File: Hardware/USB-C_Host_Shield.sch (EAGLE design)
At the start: 23 parts, among them U1 ARDUINO_UNO_R3_SHIELDBASIC, U4 AP7361C-33FGEUDFN-8, U5 MAX3421

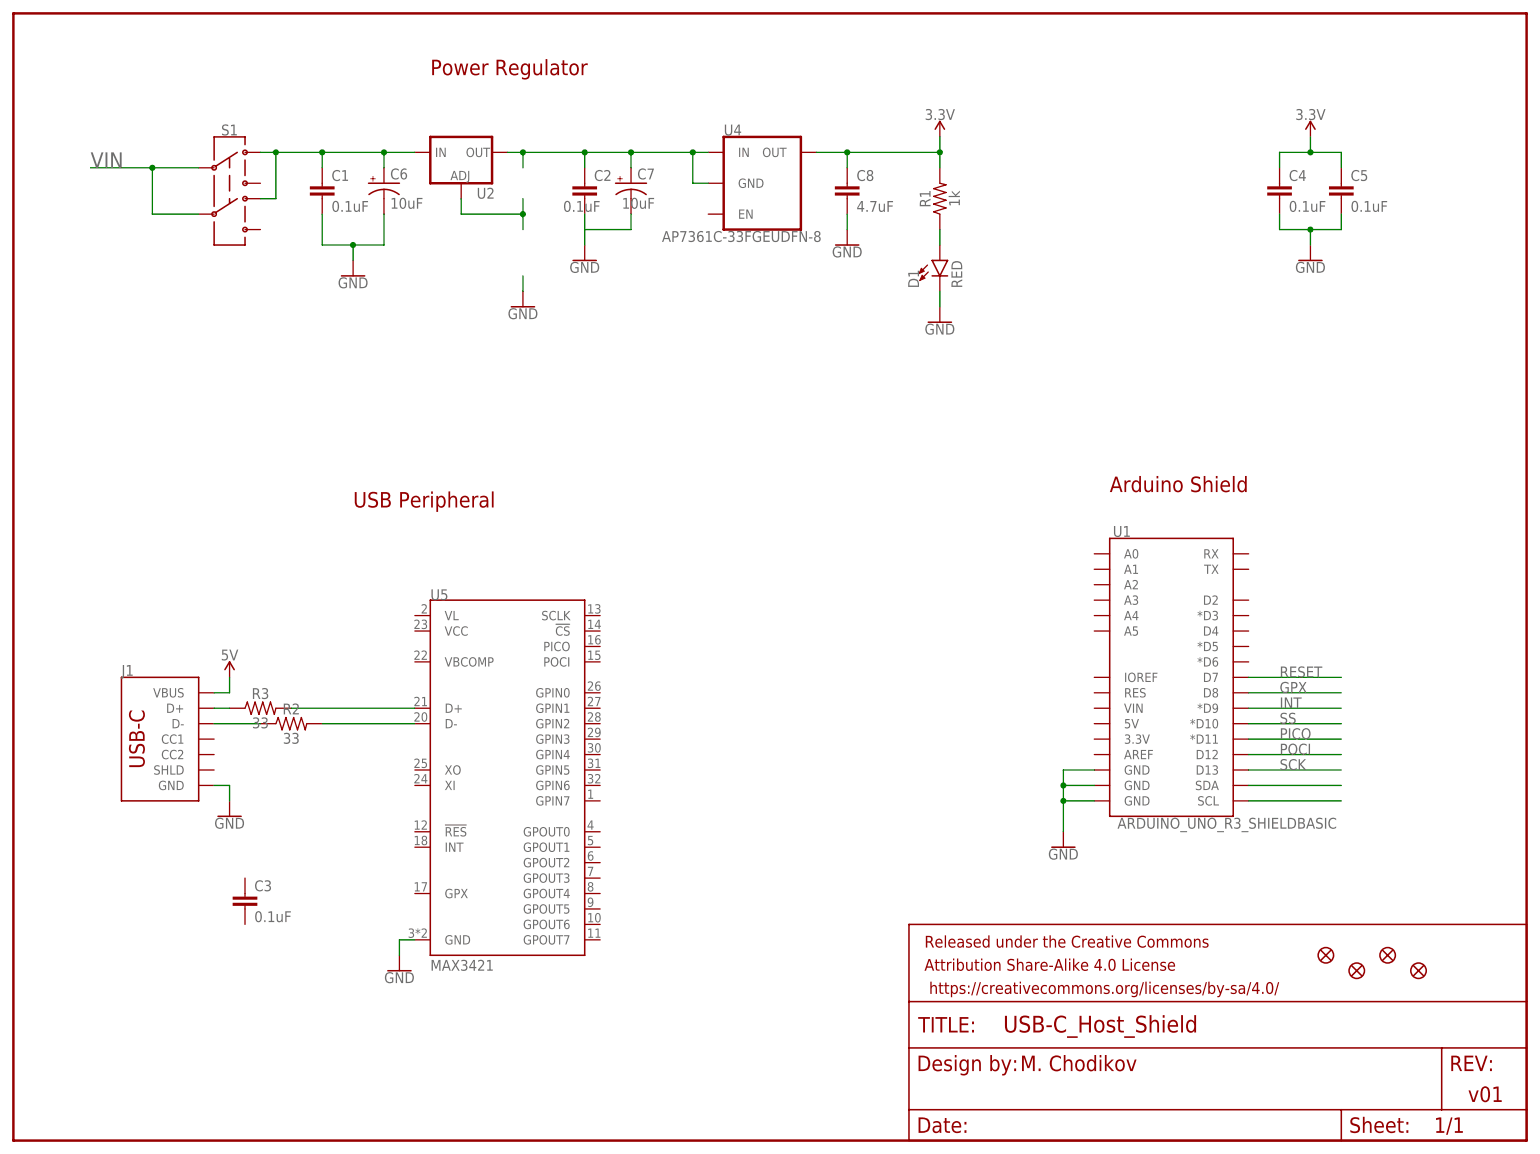
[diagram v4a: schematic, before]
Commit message: Updates to schematic, added documents
Continued work on schematic, added programming guide to documents folder
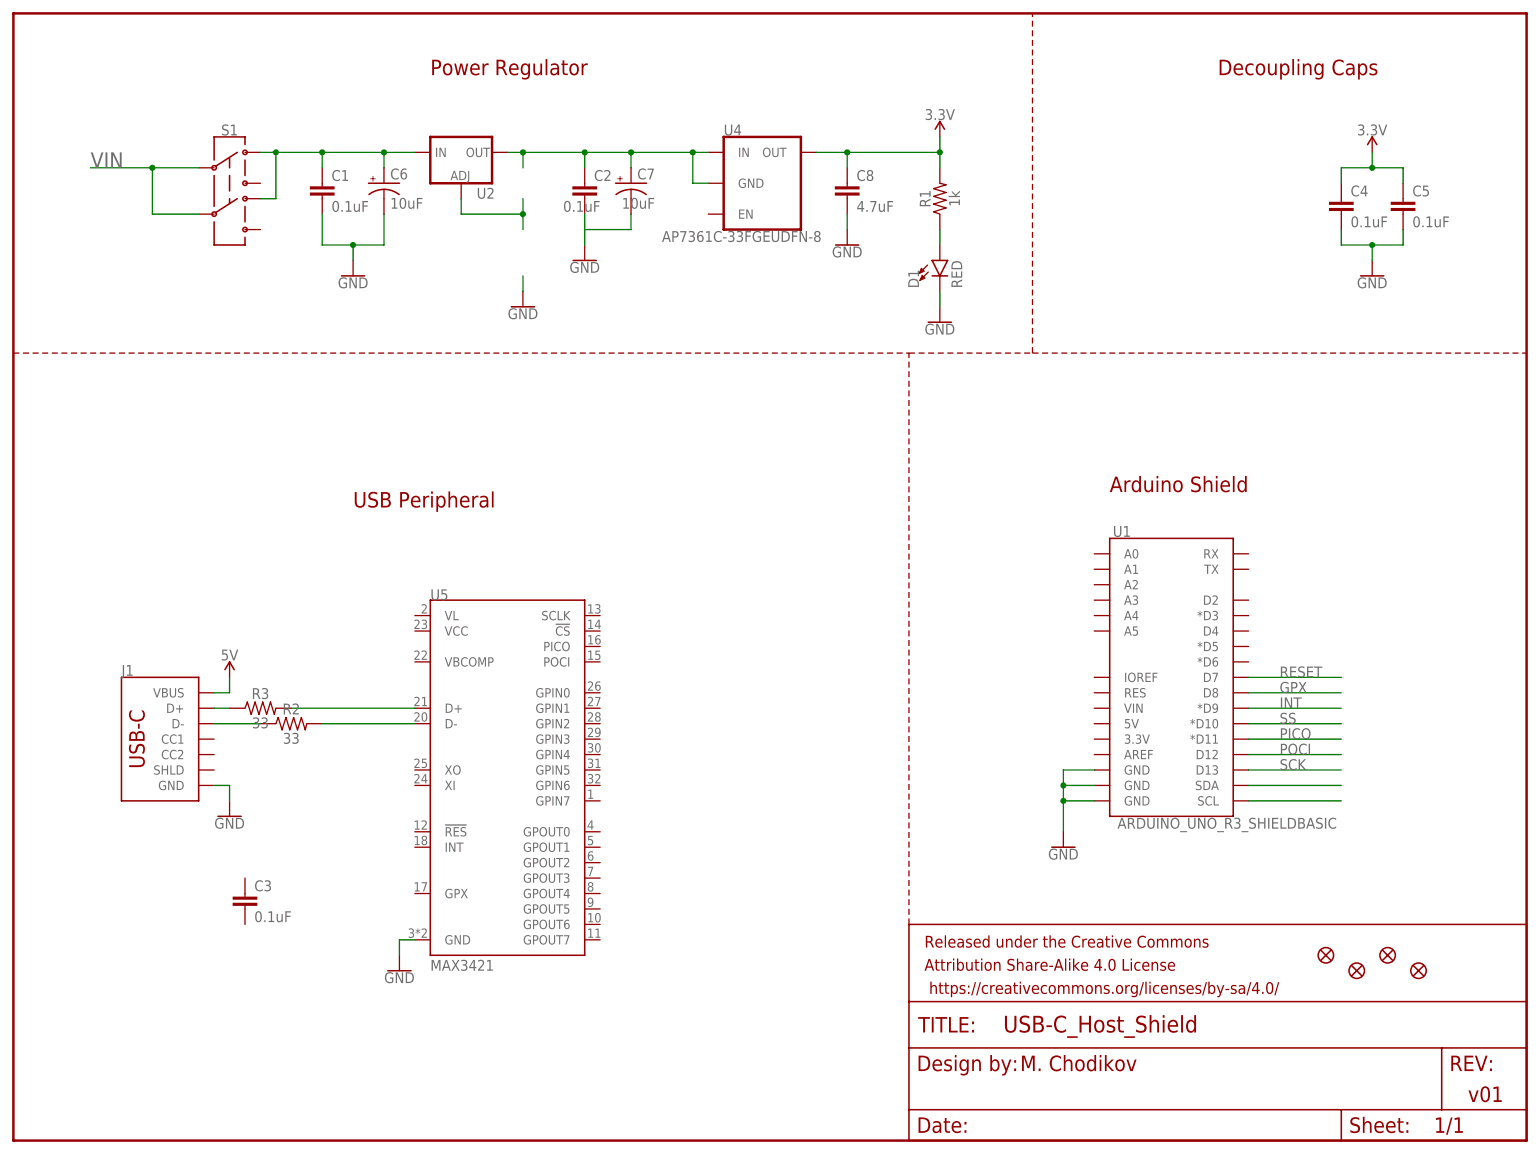
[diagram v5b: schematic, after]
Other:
- note added: "Decoupling Caps"
- moved on the sheet: C4, C5
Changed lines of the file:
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@@
 <text x="180.34" y="106.68" size="2.54" layer="94">Arduino Shield</text>
 <text x="55.88" y="104.14" size="2.54" layer="94">USB Peripheral</text>
+<wire x1="0" y1="129.54" x2="147.32" y2="129.54" width="0.2032" layer="94" style="shortdash"/>
+<wire x1="147.32" y1="129.54" x2="167.64" y2="129.54" width="0.2032" layer="94" style="shortdash"/>
+<wire x1="167.64" y1="129.54" x2="167.64" y2="185.42" width="0.2032" layer="94" style="shortdash"/>
+<wire x1="147.32" y1="35.56" x2="147.32" y2="129.54" width="0.2032" layer="94" style="shortdash"/>
+<wire x1="167.64" y1="129.54" x2="248.92" y2="129.54" width="0.2032" layer="94" style="shortdash"/>
+<text x="198.12" y="175.26" size="2.54" layer="94">Decoupling Caps</text>
 </plain>
 <instances>
@@
 <attribute name="VALUE" x="39.624" y="35.941" size="1.778" layer="96" font="vector"/>
 </instance>
-<instance part="C4" gate="G$1" x="208.28" y="154.94" smashed="yes">
-<attribute name="NAME" x="209.804" y="157.861" size="1.778" layer="95" font="vector"/>
-<attribute name="VALUE" x="209.804" y="152.781" size="1.778" layer="96" font="vector"/>
-</instance>
-<instance part="C5" gate="G$1" x="218.44" y="154.94" smashed="yes">
-<attribute name="NAME" x="219.964" y="157.861" size="1.778" layer="95" font="vector"/>
-<attribute name="VALUE" x="219.964" y="152.781" size="1.778" layer="96" font="vector"/>
-</instance>
-<instance part="SUPPLY1" gate="G$1" x="213.36" y="165.1" smashed="yes">
-<attribute name="VALUE" x="213.36" y="167.894" size="1.778" layer="96" font="vector" align="bottom-center"/>
-</instance>
-<instance part="GND1" gate="1" x="213.36" y="144.78" smashed="yes">
-<attribute name="VALUE" x="213.36" y="144.526" size="1.778" layer="96" font="vector" align="top-center"/>
+<instance part="C4" gate="G$1" x="218.44" y="152.4" smashed="yes">
+<attribute name="NAME" x="219.964" y="155.321" size="1.778" layer="95" font="vector"/>
+<attribute name="VALUE" x="219.964" y="150.241" size="1.778" layer="96" font="vector"/>
+</instance>
+<instance part="C5" gate="G$1" x="228.6" y="152.4" smashed="yes">
+<attribute name="NAME" x="230.124" y="155.321" size="1.778" layer="95" font="vector"/>
+<attribute name="VALUE" x="230.124" y="150.241" size="1.778" layer="96" font="vector"/>
+</instance>
+<instance part="SUPPLY1" gate="G$1" x="223.52" y="162.56" smashed="yes">
+<attribute name="VALUE" x="223.52" y="165.354" size="1.778" layer="96" font="vector" align="bottom-center"/>
+</instance>
+<instance part="GND1" gate="1" x="223.52" y="142.24" smashed="yes">
+<attribute name="VALUE" x="223.52" y="141.986" size="1.778" layer="96" font="vector" align="top-center"/>
 </instance>
 <instance part="GND2" gate="1" x="172.72" y="48.26" smashed="yes">
@@
 <segment>
 <pinref part="C4" gate="G$1" pin="1"/>
-<wire x1="208.28" y1="160.02" x2="208.28" y2="162.56" width="0.1524" layer="91"/>
-<wire x1="208.28" y1="162.56" x2="213.36" y2="162.56" width="0.1524" layer="91"/>
+<wire x1="218.44" y1="157.48" x2="218.44" y2="160.02" width="0.1524" layer="91"/>
+<wire x1="218.44" y1="160.02" x2="223.52" y2="160.02" width="0.1524" layer="91"/>
 <pinref part="SUPPLY1" gate="G$1" pin="3.3V"/>
-<wire x1="213.36" y1="162.56" x2="213.36" y2="165.1" width="0.1524" layer="91"/>
+<wire x1="223.52" y1="160.02" x2="223.52" y2="162.56" width="0.1524" layer="91"/>
 <pinref part="C5" gate="G$1" pin="1"/>
-<wire x1="213.36" y1="162.56" x2="218.44" y2="162.56" width="0.1524" layer="91"/>
-<wire x1="218.44" y1="162.56" x2="218.44" y2="160.02" width="0.1524" layer="91"/>
-<junction x="213.36" y="162.56"/>
+<wire x1="223.52" y1="160.02" x2="228.6" y2="160.02" width="0.1524" layer="91"/>
+<wire x1="228.6" y1="160.02" x2="228.6" y2="157.48" width="0.1524" layer="91"/>
+<junction x="223.52" y="160.02"/>
 </segment>
 <segment>
@@
 <segment>
 <pinref part="C4" gate="G$1" pin="2"/>
-<wire x1="208.28" y1="152.4" x2="208.28" y2="149.86" width="0.1524" layer="91"/>
-<wire x1="208.28" y1="149.86" x2="213.36" y2="149.86" width="0.1524" layer="91"/>
+<wire x1="218.44" y1="149.86" x2="218.44" y2="147.32" width="0.1524" layer="91"/>
+<wire x1="218.44" y1="147.32" x2="223.52" y2="147.32" width="0.1524" layer="91"/>
 <pinref part="C5" gate="G$1" pin="2"/>
-<wire x1="213.36" y1="149.86" x2="218.44" y2="149.86" width="0.1524" layer="91"/>
-<wire x1="218.44" y1="149.86" x2="218.44" y2="152.4" width="0.1524" layer="91"/>
+<wire x1="223.52" y1="147.32" x2="228.6" y2="147.32" width="0.1524" layer="91"/>
+<wire x1="228.6" y1="147.32" x2="228.6" y2="149.86" width="0.1524" layer="91"/>
 <pinref part="GND1" gate="1" pin="GND"/>
-<wire x1="213.36" y1="147.32" x2="213.36" y2="149.86" width="0.1524" layer="91"/>
-<junction x="213.36" y="149.86"/>
-</segment>
-<segment>
+<wire x1="223.52" y1="144.78" x2="223.52" y2="147.32" width="0.1524" layer="91"/>
+<junction x="223.52" y="147.32"/>
+</segment>
+<segment>

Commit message: Updated schematic
Continued work on schematic - shelving project for a little to define requirements a little more clearly
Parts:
- added C10, C9: 18pF, SparkFun-Capacitors:18PF-0603-50V-5%
- added J2, J3: (no value), SparkFun-Connectors:CONN_08"
- added R4, R5: 5.1k, SparkFun-Resistors:5.1KOHM5.1KOHM-0603-1/10W-1%
- added Y1: (no value), SparkFun-Clocks:CRYSTAL-12MHZ
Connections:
- net N$15 renamed SDA
- net N$16 renamed SCL
- new net CS_IN: U5.!CS
- new net N$12: J3.1, U5.GPOUT0
- new net N$13: J3.2, U5.GPOUT1
- new net N$14: J3.3, U5.GPOUT2
- new net N$15: J1.CC1, R5.2
- new net N$16: J1.CC2, R4.2
- new net N$17: J3.4, U5.GPOUT3
- new net N$18: J3.5, U5.GPOUT4
- new net N$19: J3.6, U5.GPOUT5
- new net N$20: J3.7, U5.GPOUT6
- new net N$21: J3.8, U5.GPOUT7
- new net N$22: J2.8, U5.GPIN7
- new net N$23: J2.7, U5.GPIN6
- new net N$24: J2.6, U5.GPIN5
- new net N$25: J2.5, U5.GPIN4
- new net N$26: J2.4, U5.GPIN3
- new net N$27: J2.3, U5.GPIN2
- new net N$28: J2.2, U5.GPIN1
- new net N$29: J2.1, U5.GPIN0
- new net N$34: C9.1, U5.XO, Y1.1
- new net N$35: U5.INT
- new net N$36: C10.1, U5.XI, Y1.2
- new net N$37: C3.1, U5.VBCOMP
- new net PICO_IN: U5.PICO
- new net RESET_IN: U5.!RES
- new net SCLK_IN: U5.SCLK
- net 3.3V: now also U5.VCC, U5.VL
- net GND: now also C10.2, C3.2, C9.2, R4.1, R5.1
- net GPX: now also U5.GPX
- net POCI: now also U5.POCI
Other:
- moved on the sheet: C1, C2, C3, C4, C5, C6, C7, C8, D1, J1, R1, R2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

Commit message: Continued work on Layout
Verify again 9/21 morning, but this should be nearly ready for layout
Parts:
- removed U4: AP7361C-33FGEUDFN-8, SparkFun-IC-Power:AP7361C-33FGEUDFN-8
- added F1: 6V/0.5A, SparkFun-Fuses:PPTC_6V500MA-2
- added R6: 2.2k, SparkFun-Resistors:2.2KOHM-0603-1/10W-1%
- added R7: 715, SparkFun-Resistors:715OHM-0603-1/10W-1%
- added R8: 240, SparkFun-Resistors:240OHM-0603-1/10W-1%
- added S2: MOMENTARY-SWITCH-SPST-SMD-5.2MM-TALL, SparkFun-Switches:MOMENTARY-SWITCH-SPST-SMD-5.2MM-TALL
- added U3: 74HC4050, SparkFun-IC-Comms:HEX_CONVERTER
- added U6: 3.3V/150mA, SparkFun-IC-Power:V_REG_MIC52053.3V
- C8: value 4.7uF -> 10uF; device SparkFun-Capacitors:4.7UF-0603-6.3V-(10%) -> SparkFun-Capacitors:10UF-0603-6.3V-20%
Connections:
- net SCLK_IN renamed SCK_IN
- removed net CS_IN: U5.!CS
- removed net N$35: U5.INT
- removed net PICO_IN: U5.PICO
- removed net SCL: U1.SCL
- removed net SDA: U1.SDA
- removed net SS: U1.*D10
- new net CS: U1.*D10, U3.2A
- new net CS-IN: U3.2Y, U5.!CS
- new net N$30: S2.2, U1.RES
- new net N$31: F1.1, J1.VBUS
- new net N$5: R7.1
- new net PICO-IN: U3.3Y, U5.PICO
- new net RESET-IN: U3.4Y
- new net SCK-IN: U3.1Y
- net 3.3V: now also R6.2, U3.VCC, U6.OUT; no longer U4.OUT
- net 5V: now also F1.2; no longer J1.VBUS
- net GND: now also S2.1, U3.GND, U6.GND
- net INT: now also R6.1, U5.INT
- net N$3: now also R8.2, U6.EN, U6.IN; no longer U4.GND, U4.IN
- net N$4: now also R7.2, R8.1
- net PICO: now also U3.3A
- net RESET: now also U3.4A
- net SCK: now also U3.1A
- net VIN: now also U1.VIN
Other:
- note added: "Hex Inverter"
- note removed: "Decoupling Caps"
- moved on the sheet: C10, C3, C4, C5, C9, J1, J2, J3, R2, R3, R4, R5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

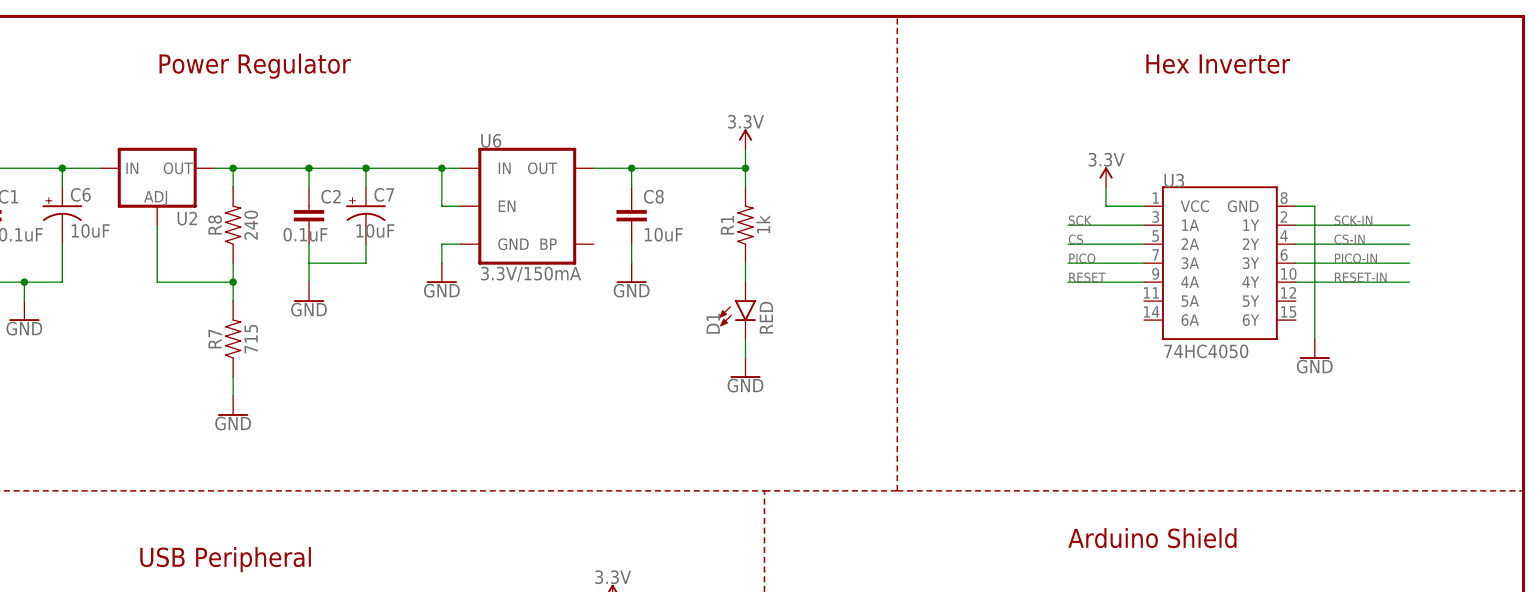
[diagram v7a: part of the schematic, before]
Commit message: Verified schematic and created layout
Created layout document after verifying all schematic sections with datasheets.
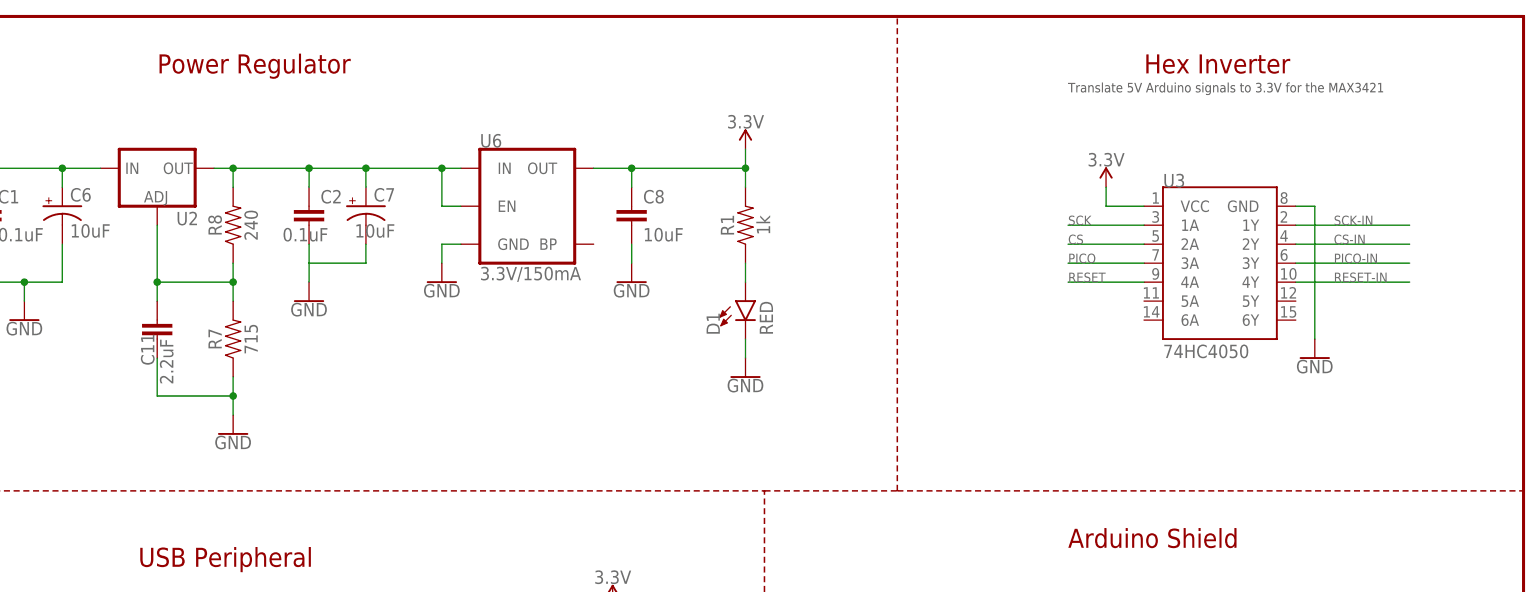
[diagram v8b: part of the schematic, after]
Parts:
- added C11: 2.2uF, SparkFun-Capacitors:2.2UF-0603-10V-20%
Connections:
- net N$4: now also C11.1
- net N$5: now also C11.2
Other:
- note added: "Translate 5V Arduino signals to 3.3V for the MAX3421"
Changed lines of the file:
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@@
 <part name="C8" library="SparkFun-Capacitors" deviceset="10UF" device="-0603-6.3V-20%" value="10uF"/>
 <part name="R8" library="SparkFun-Resistors" deviceset="240OHM" device="-0603-1/10W-1%" value="240"/>
+<part name="C11" library="SparkFun-Capacitors" deviceset="2.2UF" device="-0603-10V-20%" value="2.2uF"/>
 </parts>
 <sheets>
@@
 <wire x1="165.1" y1="121.92" x2="248.92" y2="121.92" width="0.2032" layer="94" style="shortdash"/>
 <text x="198.12" y="177.8" size="2.54" layer="94">Hex Inverter</text>
+<text x="187.96" y="175.26" size="1.27" layer="97">Translate 5V Arduino signals to 3.3V for the MAX3421</text>
 </plain>
 <instances>
@@
 <attribute name="VALUE" x="146.304" y="157.48" size="1.778" layer="96" font="vector" rot="R90" align="top-center"/>
 </instance>
-<instance part="GND4" gate="1" x="76.2" y="132.08" smashed="yes">
-<attribute name="VALUE" x="76.2" y="131.826" size="1.778" layer="96" font="vector" align="top-center"/>
+<instance part="GND4" gate="1" x="76.2" y="129.54" smashed="yes">
+<attribute name="VALUE" x="76.2" y="129.286" size="1.778" layer="96" font="vector" align="top-center"/>
 </instance>
 <instance part="SUPPLY2" gate="G$1" x="144.78" y="167.64" smashed="yes">
@@
 <attribute name="NAME" x="74.676" y="157.48" size="1.778" layer="95" font="vector" rot="R90" align="bottom-center"/>
 <attribute name="VALUE" x="77.724" y="157.48" size="1.778" layer="96" font="vector" rot="R90" align="top-center"/>
+</instance>
+<instance part="C11" gate="G$1" x="66.04" y="142.24" smashed="yes">
+<attribute name="NAME" x="65.659" y="138.684" size="1.778" layer="95" font="vector" rot="R90"/>
+<attribute name="VALUE" x="68.199" y="136.144" size="1.778" layer="96" font="vector" rot="R90"/>
 </instance>
 </instances>
@@
 <wire x1="76.2" y1="149.86" x2="76.2" y2="152.4" width="0.1524" layer="91"/>
 <junction x="76.2" y="149.86"/>
+<pinref part="C11" gate="G$1" pin="1"/>
+<wire x1="66.04" y1="149.86" x2="66.04" y2="147.32" width="0.1524" layer="91"/>
+<junction x="66.04" y="149.86"/>
 </segment>
 </net>
@@
 <pinref part="R7" gate="G$1" pin="1"/>
 <wire x1="76.2" y1="137.16" x2="76.2" y2="134.62" width="0.1524" layer="91"/>
-</segment>
-</net>
+<pinref part="C11" gate="G$1" pin="2"/>
+<wire x1="76.2" y1="134.62" x2="76.2" y2="132.08" width="0.1524" layer="91"/>
+<wire x1="66.04" y1="139.7" x2="66.04" y2="134.62" width="0.1524" layer="91"/>
+<wire x1="66.04" y1="134.62" x2="76.2" y2="134.62" width="0.1524" layer="91"/>
+<junction x="76.2" y="134.62"/>
+</segment>
+</net>
